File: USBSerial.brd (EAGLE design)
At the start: 44.5 x 25.4 mm, 27 parts, among them IC1 ATMEGA16U2 QFN-32, J1 Gnd, J2 DFU

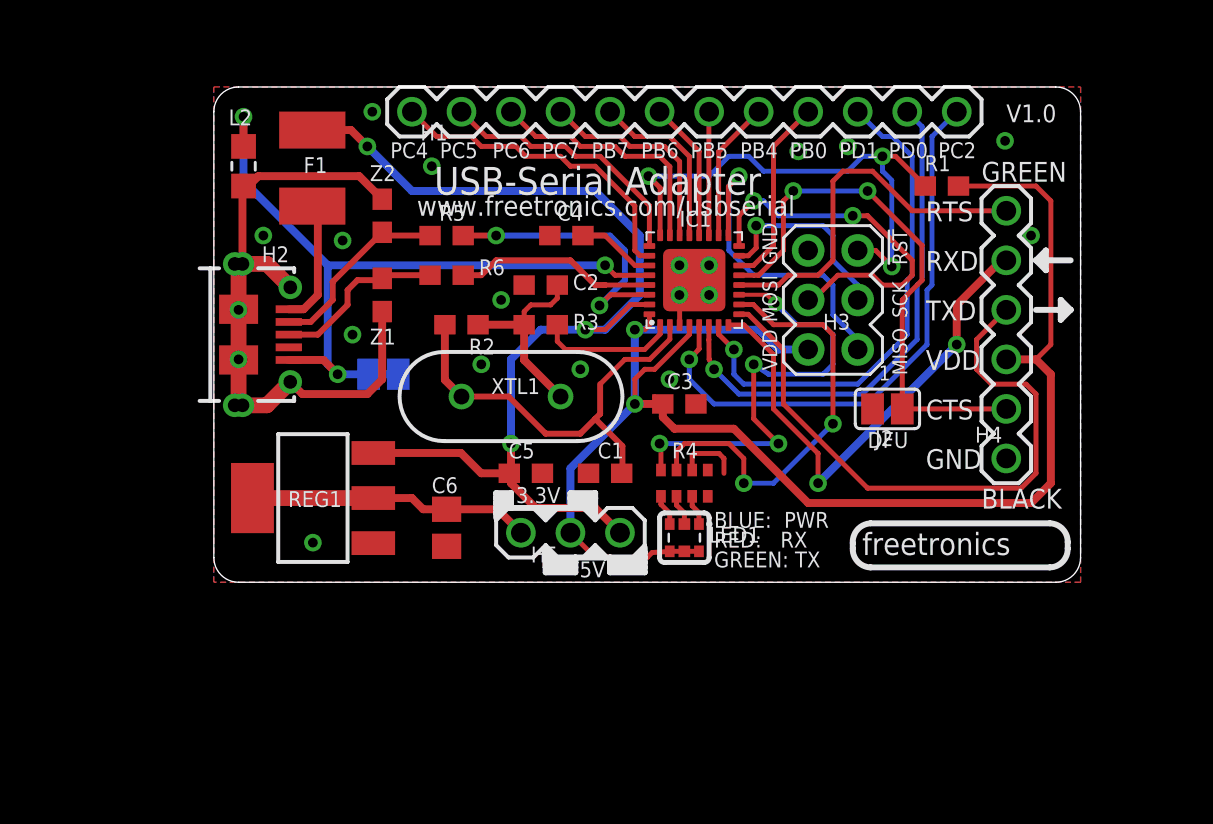
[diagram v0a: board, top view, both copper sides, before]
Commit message: Changed CTS / RTS assignment
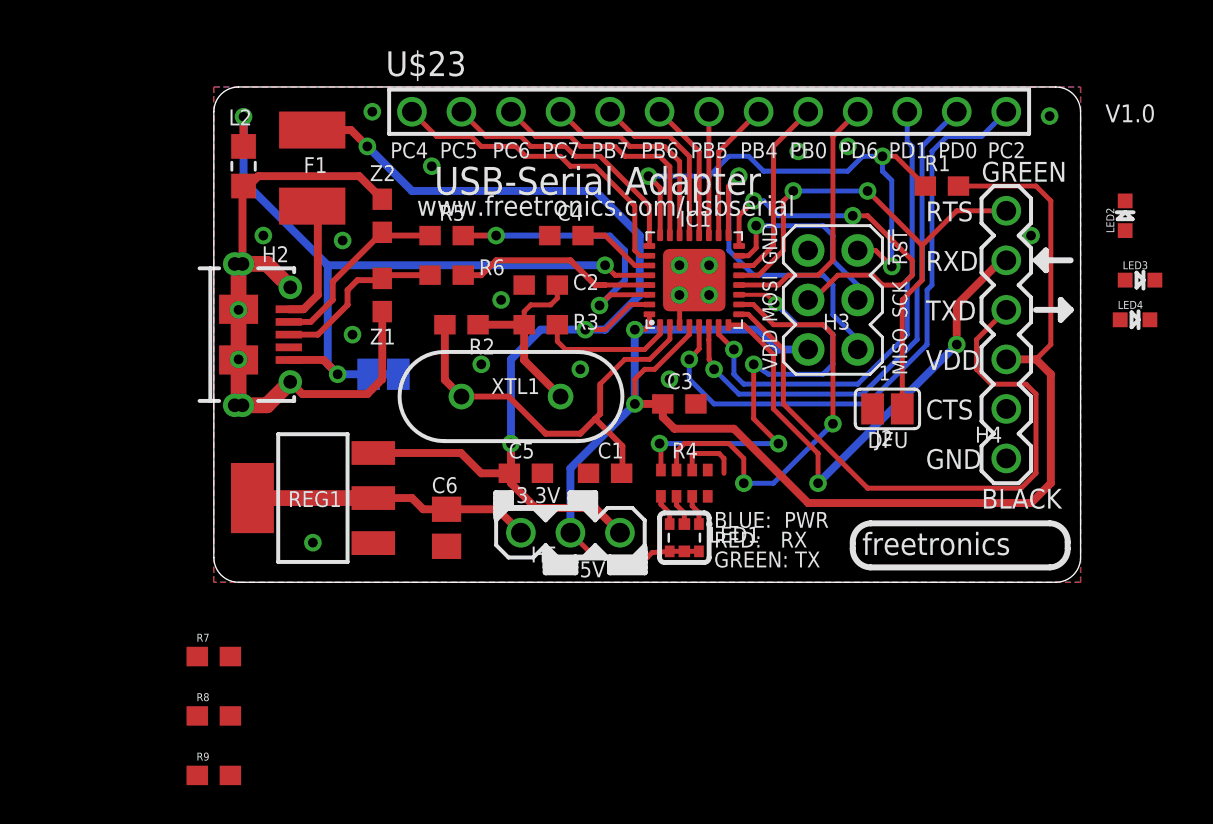
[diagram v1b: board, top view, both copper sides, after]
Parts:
- removed H1: M12PTH, freetronics-original:1X12
- added LED2, LED3, LED4: (no value), freetronics-jon:LED-0603
- added R7, R8, R9: 1K 0603, freetronics:0603
- added U$23: M13, freetronics-jon:1X13
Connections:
- removed net RTS: H4.6, IC1.12
- new net N$3: LED2.C, R7.2
- new net N$7: LED4.C, R8.2
- new net N$9: LED3.C, R9.2
- new net PD6: IC1.12, U$23.10
- net CTS: now also H4.6; no longer H4.2
- net PB0: now also U$23.9; no longer H1.9
- net PB4: now also U$23.8; no longer H1.8
- net PB5: now also U$23.7; no longer H1.7
- net PB6: now also U$23.6; no longer H1.6
- net PB7: now also U$23.5; no longer H1.5
- net PC2: now also U$23.13; no longer H1.12
- net PC4: now also U$23.1; no longer H1.1
- net PC5: now also U$23.2; no longer H1.2
- net PC6: now also U$23.3; no longer H1.3
- net PC7: now also U$23.4; no longer H1.4
- net PD0: now also U$23.12; no longer H1.11
- net PD1: now also U$23.11; no longer H1.10
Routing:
- net RTS: track 19.3 -> 0.00 mm
- net PD6: track 0.00 -> 13.5 mm
- net PC2: track 29.5 -> 31.6 mm
- net PD1: track 26.0 -> 24.6 mm
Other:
- board text added: "PD6"

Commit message: v1.1 release: Separate LEDs near TX/RX/VCC pins; PCB tab over connector; label improvements
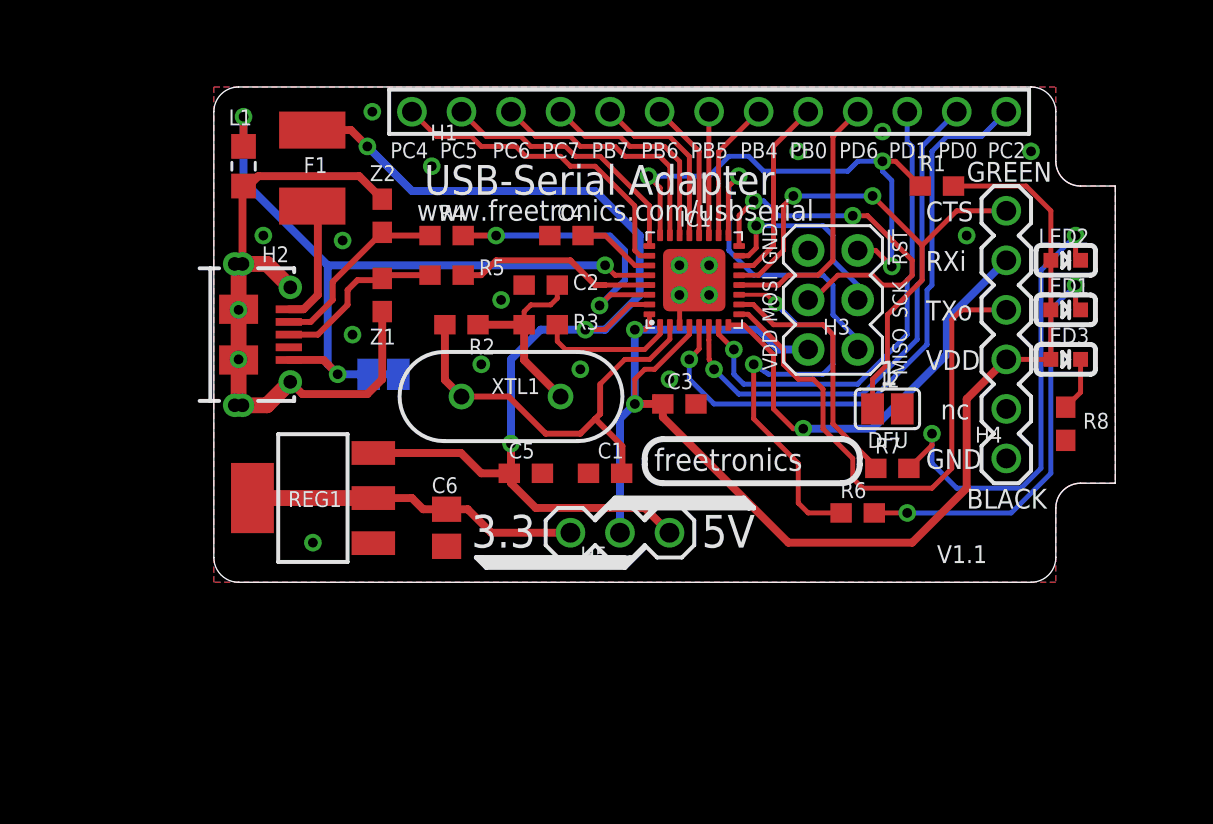
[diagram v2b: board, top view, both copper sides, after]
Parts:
- removed LED4: (no value), freetronics-jon:LED-0603
- removed R9: 1K 0603, freetronics:0603
- LED1: value RGB -> GREEN 0603; device freetronics-master-v1:19-337 -> freetronics-jon:LED-0603
- LED2: value (none) -> RED 0603
- LED3: value (none) -> BLUE 0603
- R4: value 1k -> 22R 0603; device freetronics-luke:CAY16 -> freetronics:0603
- R6: value 22R 0603 -> 1K 0603
- moved R8 46.2 mm to (43.7, 8.13), turned to 90 degrees
- moved R7 36.1 mm to (34.8, 5.84)
- moved R6 24.4 mm to (33.0, 3.56), turned to 0 degrees
- moved LED1 22.8 mm to (43.7, 14.0), turned to 0 degrees
- moved R4 17.6 mm to (11.9, 17.8), turned to 180 degrees
- moved LED3 5.57 mm to (43.7, 11.4)
- moved LED2 3.81 mm to (43.7, 16.5), turned to 0 degrees
- moved H5 2.54 mm to (20.8, 2.54)
- moved R5 2.03 mm to (11.9, 15.7)
- moved R1 0.25 mm to (37.1, 20.3)
- turned J2 to 180 degrees
- renumbered L2 to L1, U$23 to H1
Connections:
- removed net N$4: LED1.2, R4.2
- removed net N$5: LED1.1, R4.3
- removed net N$6: LED1.3, R4.1
- removed net N$7 (its old number): LED4.C, R8.2
- new net N$3: LED1.C, R6.2
- net GND: now also R8.1; no longer R4.6
- net N$16: now also R5.2; no longer R6.2
- net N$17: now also R4.2; no longer R5.2
- net N$9: now also R8.2; no longer R9.2
- net RD+: now also R5.1; no longer R6.1
- net RD-: now also R4.1; no longer R5.1
- net RXLED: now also R7.1; no longer R4.7
- net TXLED: now also R6.1; no longer R4.8
- net VDD: now also LED1.A, LED2.A, LED3.A; no longer LED1.4, LED1.5, LED1.6
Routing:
- net N$7: track 0.00 -> 24.6 mm, vias 0 -> 2
- net N$3: track 0.00 -> 21.5 mm, vias 0 -> 2
- net VDD: track 82.1 -> 72.3 mm
- net RXLED: track 22.0 -> 13.3 mm, vias 2 -> 0
- net TXD: track 32.2 -> 27.9 mm
- net RXD: track 26.0 -> 22.7 mm, vias 2 -> 1
- net GND: track 6.56 -> 3.27 mm
- net N$9: track 0.00 -> 2.77 mm
- net +5V: track 54.4 -> 56.9 mm
- net +3V3: track 14.5 -> 17.0 mm
- net N$6: track 1.68 -> 0.00 mm
- net TXLED: track 23.7 -> 22.1 mm, vias 4 -> 2
- net N$4: track 1.59 -> 0.00 mm
- net N$5: track 1.56 -> 0.00 mm
- net !RESET: track 27.4 -> 26.9 mm
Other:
- board size 44.5 x 25.4 mm -> 46.2 x 25.4 mm
- board text added: "3.3"
- board text added: "A"
- board text added: "K"
- board text added: "RXi"
- board text added: "SKU: USBSERIAL"
- board text added: "TXo"
- board text added: "V1.1"
- board text added: "nc"
- board text removed: "3.3V"
- board text removed: "BLUE: PWR"
- board text removed: "GREEN: TX"
- board text removed: "LED1"
- board text removed: "RED: RX"
- board text removed: "RTS"
- board text removed: "RXD"
- board text removed: "SKU:USBSERIAL"
- board text removed: "TXD"
- board text removed: "V1.0"

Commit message: Minor cleanups for v1.2 release
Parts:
- removed H5: VDD Select, freetronics-luke:JUMPER_SPDT
- added SW1: MK-12C02-PB, freetronics-jon:MK-12C02
- XTL1: device freetronics-master-v1:HC49US -> freetronics-jon:HC49U-V
- moved C5 9.18 mm to (24.9, 3.30), turned to 270 degrees
- moved R6 3.97 mm to (30.0, 6.10)
- moved C1 3.94 mm to (23.9, 6.60), turned to 180 degrees
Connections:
- net +3V3: now also SW1.1; no longer H5.1
- net +5V: now also SW1.3; no longer H5.3
- net GND: now also SW1.MNT@1, SW1.MNT@2, SW1.MNT@3, SW1.MNT@4
- net VDD: now also SW1.2; no longer H5.2
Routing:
- net TXLED: track 22.1 -> 17.3 mm
- net N$3: track 21.5 -> 26.2 mm
- net VDD: track 72.3 -> 70.6 mm, vias 2 -> 3
- net +5V: track 56.9 -> 58.3 mm
- net +3V3: track 17.0 -> 16.4 mm
- net GND: vias 18 -> 22
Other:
- outline, holes or cut-outs redrawn
- board text added: "RX"
- board text added: "TX"
- board text added: "V1.2"
- board text added: "VOUT"
- board text removed: "RXi"
- board text removed: "TXo"
- board text removed: "V1.1"

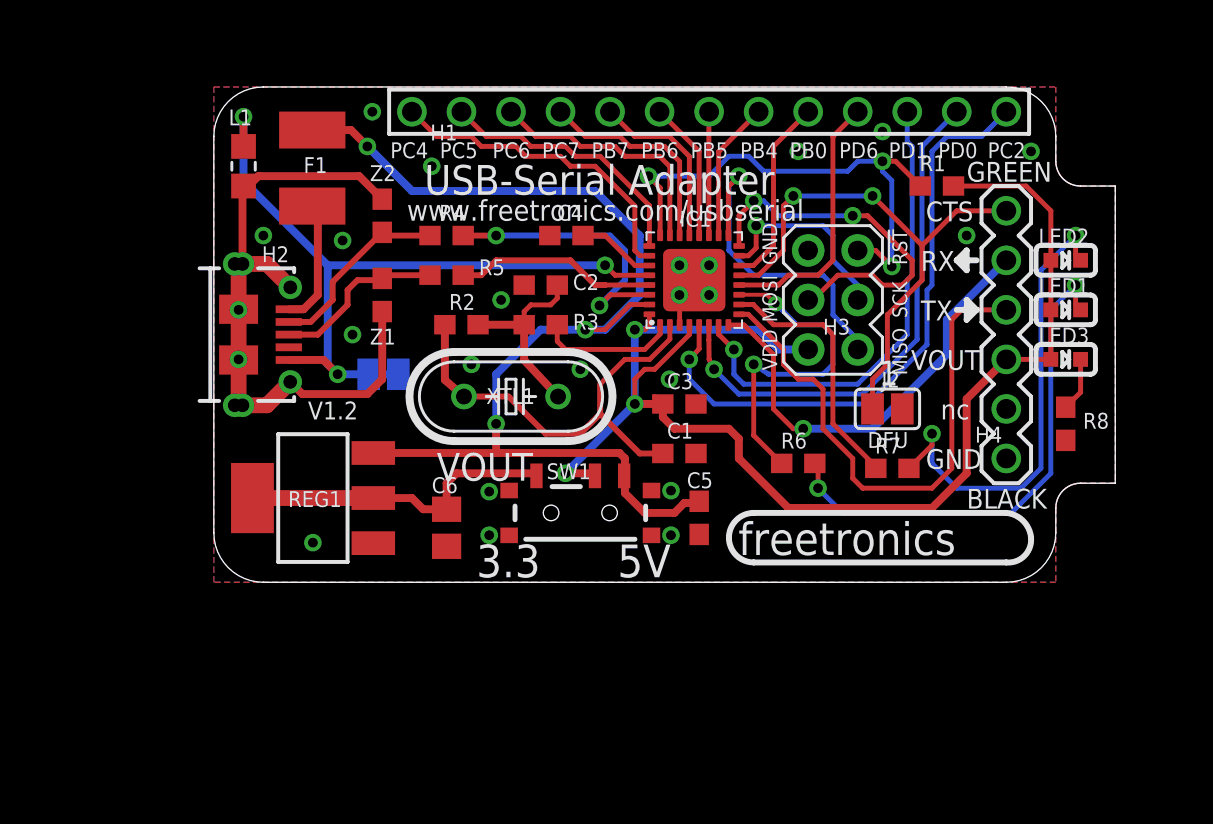
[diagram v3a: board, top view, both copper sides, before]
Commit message: Replaced USB connector with USB-C
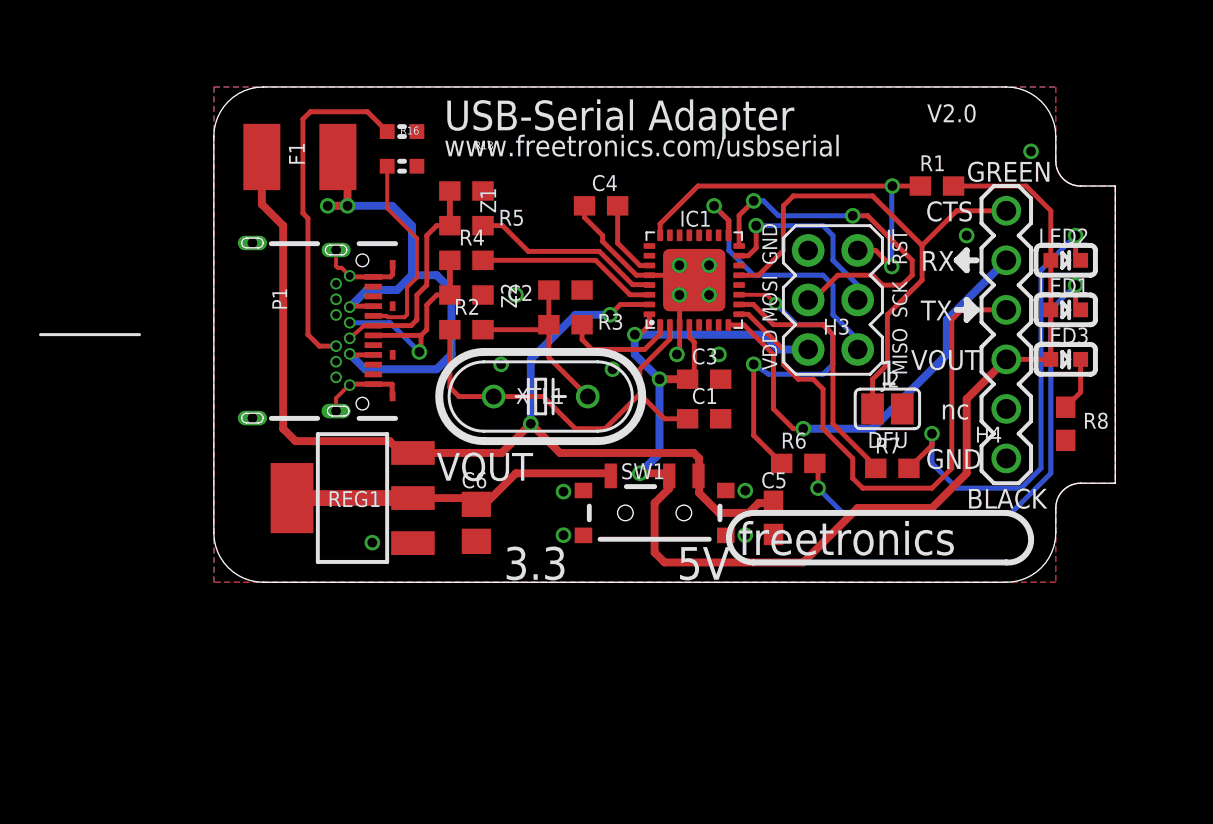
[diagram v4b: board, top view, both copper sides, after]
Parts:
- removed H1: M13, freetronics-jon:1X13
- removed H2: USB-6PSMT, freetronics-jon:USB-MICROB-MB05PMXX
- removed J1: Gnd, freetronics-jon:SJC
- removed L1: 0805 INDUCTOR, freetronics-master-v1:0805-LARGE
- added P1: USB-C, freetronics-jon:USB-C-U52A
- added R16, R18: 5.1K, freetronics-original:0603
- moved Z1 6.86 mm to (13.0, 20.1), turned to 0 degrees
- moved Z2 5.93 mm to (13.0, 14.7), turned to 0 degrees
- moved C5 3.81 mm to (28.7, 3.30)
- moved SW1 3.81 mm to (22.6, 3.56)
- moved R5 2.74 mm to (13.0, 18.3)
- moved C4 2.34 mm to (19.9, 19.3)
- moved C1 2.18 mm to (25.1, 8.38)
- moved REG1 2.03 mm to (7.11, 4.32)
- moved C3 1.80 mm to (25.1, 10.4)
- moved R4 1.63 mm to (13.0, 16.5)
- moved C6 1.55 mm to (13.5, 3.05)
- moved XTL1 1.52 mm to (16.8, 9.53)
- moved C2 1.30 mm to (18.0, 15.0), turned to 180 degrees
- moved R3 1.27 mm to (18.0, 13.2)
- moved F1 0.85 mm to (4.41, 21.8), turned to 180 degrees
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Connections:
- removed net N$1: H2.GND, IC1.28, J1.2, L1.1
- removed net N$115: F1.1, H2.VBUS
- removed net N$16: H2.D+, R5.2, Z1.1
- removed net N$17: H2.D-, R4.2, Z2.1
- removed net N$8: H2.FIX1, H2.FIX2, H2.PIN1, H2.PIN2, H2.TAB1, H2.TAB2, L1.2, Z1.2, Z2.2
- new net D+: P1.A6, P1.B6, R5.2, Z1.1
- new net D-: P1.A7, P1.B7, R4.2, Z2.1
- new net N$4: P1.A5, R16.2
- new net N$5: P1.B5, R18.2
- new net USB+: F1.1, P1.A4, P1.A9, P1.B4, P1.B9
- net GND: now also IC1.28, P1.A1, P1.A12, P1.B1, P1.B12, P1.CASE1, P1.CASE2, P1.CASE3, P1.CASE4, P1.FIX1, P1.FIX2, P1.FIX3, P1.FIX4, R16.1, R18.1, Z1.2, Z2.2; no longer J1.1
- net PB0: no longer H1.9
- net PB4: no longer H1.8
- net PB5: no longer H1.7
- net PB6: no longer H1.6
- net PB7: no longer H1.5
- net PC2: no longer H1.13
- net PC4: no longer H1.1
- net PC5: no longer H1.2
- net PC6: no longer H1.3
- net PC7: no longer H1.4
- net PD0: no longer H1.12
- net PD1: no longer H1.11
- net PD6: no longer H1.10
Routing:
- net N$1: track 37.8 -> 0.00 mm, vias 3 -> 0
- net N$8: track 34.0 -> 0.00 mm, vias 2 -> 0
- net PC2: track 31.6 -> 0.00 mm, vias 1 -> 0
- net USB+: track 0.00 -> 28.9 mm, vias 0 -> 2
- net PD0: track 27.0 -> 0.00 mm, vias 1 -> 0
- net PD1: track 24.6 -> 0.00 mm, vias 1 -> 0
- net N$5: track 0.00 -> 17.7 mm
- net GND: track 3.27 -> 21.0 mm, vias 22 -> 16
- net PC4: track 16.6 -> 0.00 mm
- net PC5: track 13.7 -> 0.00 mm
- net PD6: track 13.5 -> 0.00 mm
- net PC6: track 12.8 -> 0.00 mm
- net D-: track 0.00 -> 12.4 mm, vias 0 -> 1
- net D+: track 0.00 -> 11.5 mm
- net PC7: track 10.9 -> 0.00 mm
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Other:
- board text added: "V2.0"
- board text removed: "PB0"
- board text removed: "PB4"
- board text removed: "PB5"
- board text removed: "PB6"
- board text removed: "PB7"
- board text removed: "PC2"
- board text removed: "PC4"
- board text removed: "PC5"
- board text removed: "PC6"
- board text removed: "PC7"
- board text removed: "PD0"
- board text removed: "PD1"
- board text removed: "PD6"
- board text removed: "V1.2"
